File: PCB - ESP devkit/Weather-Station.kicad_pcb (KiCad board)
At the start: 2 copper layers, 39 parts, among them J1 Biruta, J10 Conn_01x19, J11 Conn_01x19, J2 Power, J3 BH1750-FVI, J4 BME280, J5 Pluviometro, J6 Anemometro, J7 FTDI, J8 Conn_01x02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

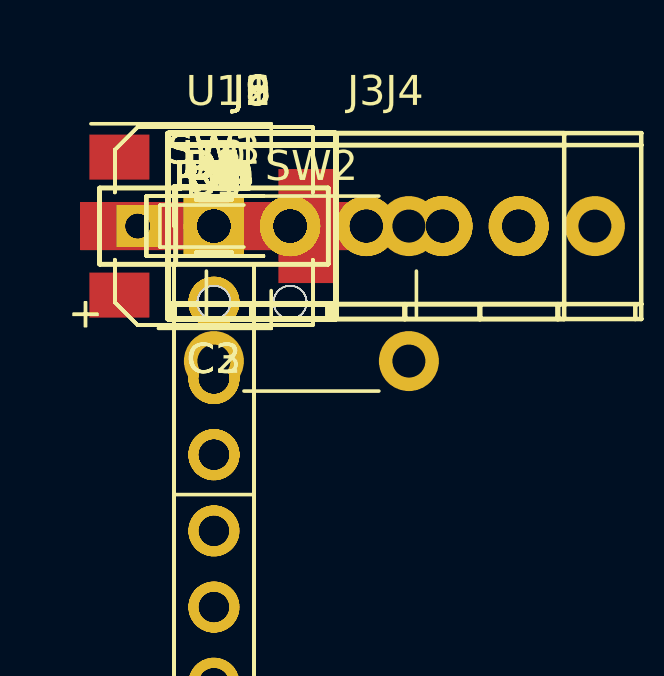
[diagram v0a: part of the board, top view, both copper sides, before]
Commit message: Tirando o circuito de programação do ESP
Signed-off-by: Gustavo Costa <gustavocosta@ic.ufal.br>
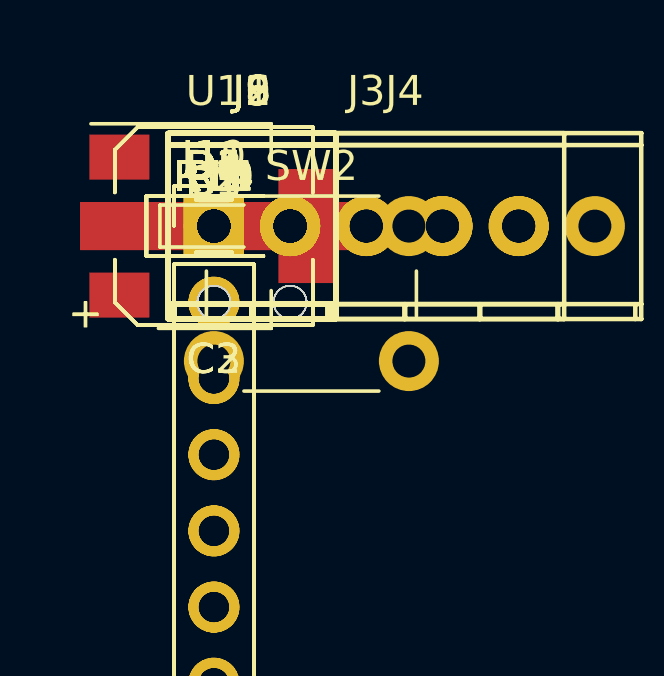
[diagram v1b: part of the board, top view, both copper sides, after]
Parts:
- removed J7: FTDI, Pin_Headers:Pin_Header_Straight_1x04_Pitch2.54mm
- removed R16, R4, R6, R8: 10K, Resistors_SMD:R_0805
- removed SW1: SW_Push_SPDT, Buttons_Switches_ThroughHole:SW_Micro_SPST
- removed SW3: SW_SPDT, Buttons_Switches_ThroughHole:SW_Micro_SPST
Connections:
- C3 pad 1: Net-(C3-Pad1) -> +3V3
- J10 pad 13: Net-(J10-Pad13) -> (no net)
- J11 pad 15: RXD -> (no net)
- J11 pad 16: TXD -> (no net)
- J11 pad 4: Net-(J11-Pad4) -> (no net)
- J11 pad 5: Net-(J11-Pad5) -> (no net)
- J11 pad 6: Net-(J11-Pad6) -> (no net)
- U1 pad 2: Net-(C3-Pad1) -> +3V3

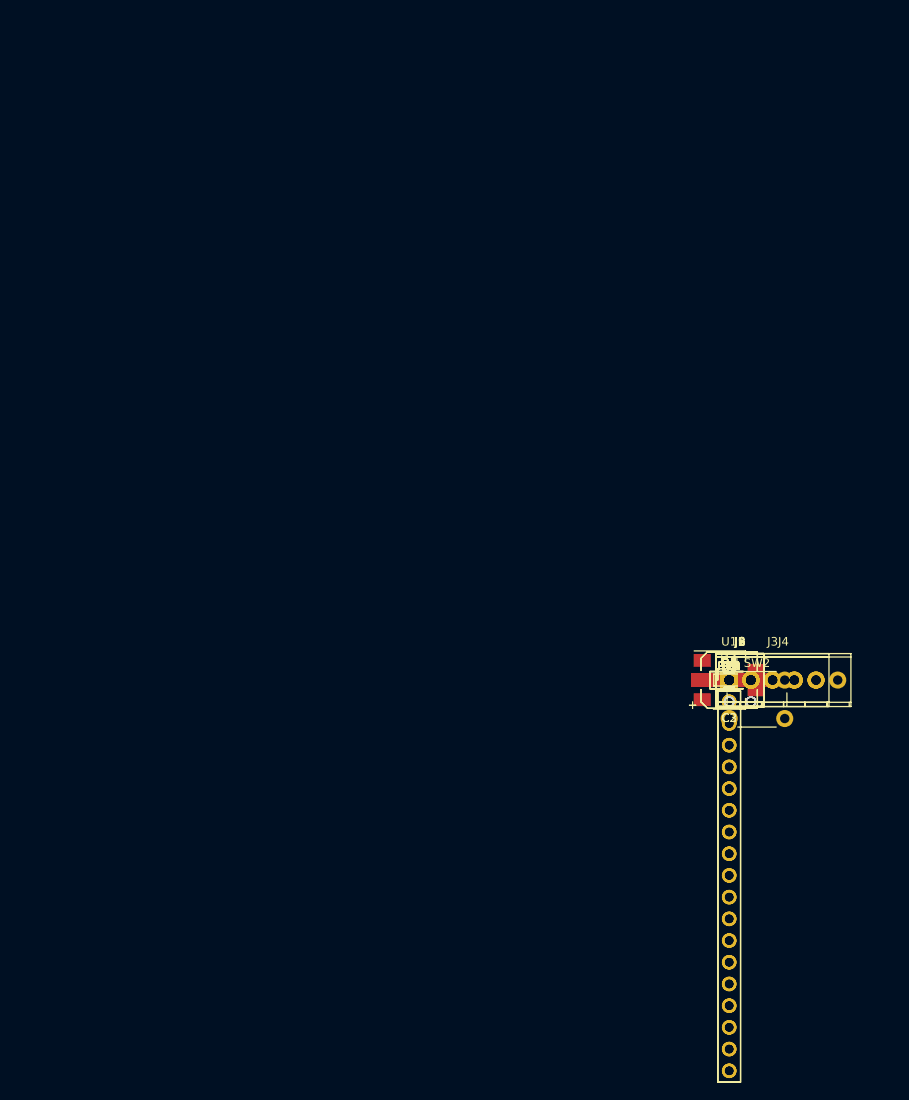
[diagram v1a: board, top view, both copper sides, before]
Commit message: Feita a PCB com ESP32 devkit
Signed-off-by: Gustavo Costa <gustavocosta@ic.ufal.br>
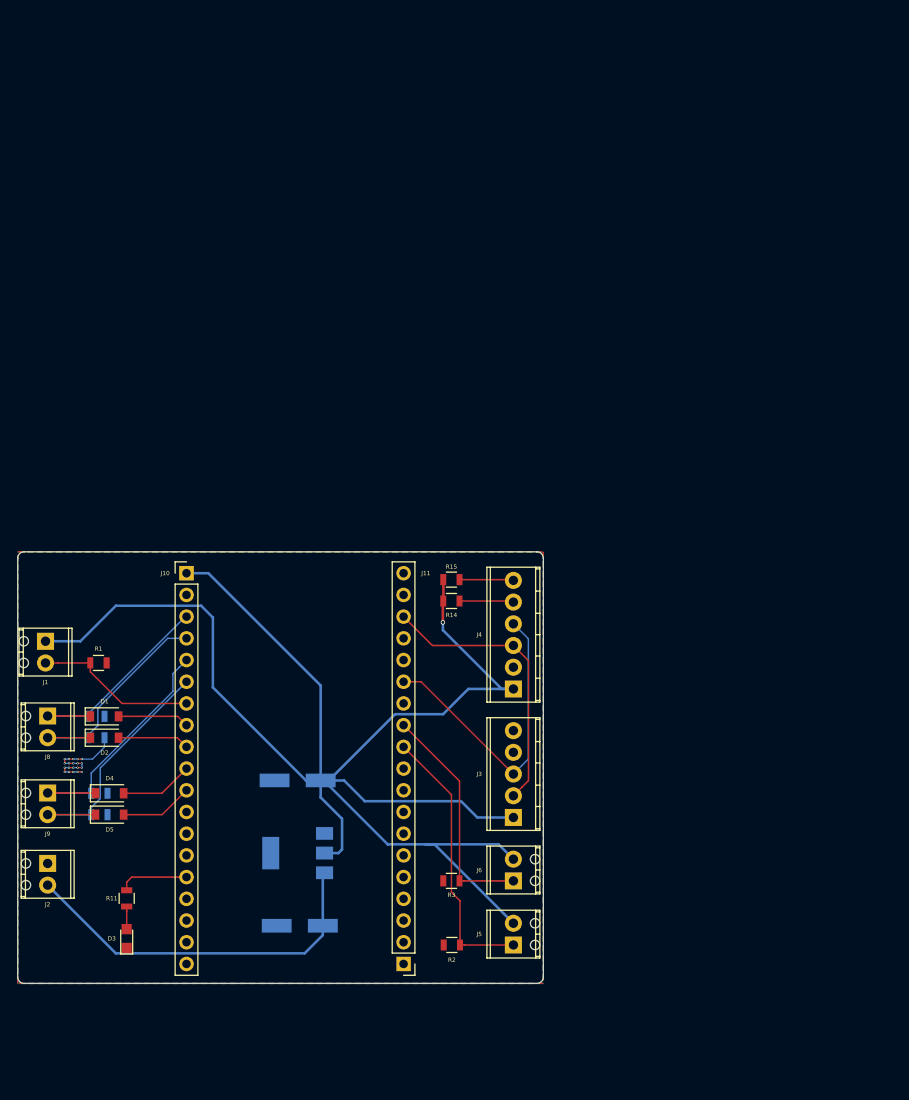
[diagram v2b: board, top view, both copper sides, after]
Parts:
- removed C1: 100nF, Capacitors_SMD:C_0805
- removed R5, R7: 10K, Resistors_SMD:R_0805
- removed SW2: SW_Push, Buttons_Switches_THT:SW_PUSH_6mm
- C2, C3, R10, R12, R13, R9, U1: moved to B.Cu
- moved J2 82.6 mm to (68.8, 126.5), turned to 270 degrees
- moved J9 80.8 mm to (68.8, 118.2), turned to 270 degrees
- moved J1 80.1 mm to (68.5, 100.5), turned to 270 degrees
- moved J8 79.9 mm to (68.8, 109.2), turned to 270 degrees
- moved D3 76.7 mm to (78.0, 135.2), turned to 90 degrees
- moved R13 75.4 mm to (74.8, 120.8)
- moved R11 75.0 mm to (78.0, 130.6), turned to 270 degrees
- moved R12 74.9 mm to (74.8, 118.2)
- moved R10 74.4 mm to (74.5, 111.8)
- moved D5 74.2 mm to (76.0, 120.8)
- moved R9 74.2 mm to (74.5, 109.2)
- moved R1 73.8 mm to (74.7, 103.0)
- moved D4 73.7 mm to (76.0, 118.2)
- moved D2 73.4 mm to (75.4, 111.8)
- moved D1 73.2 mm to (75.4, 109.2)
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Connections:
- J10 pad 2: Net-(C1-Pad2) -> (no net)
- J11 pad 10: Net-(J11-Pad10) -> (no net)
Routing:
- net +3V3: track 0.00 -> 200.5 mm, vias 0 -> 1
- net Net-(C2-Pad1): track 0.00 -> 43.8 mm
- net Net-(J11-Pad14): track 0.00 -> 36.4 mm
- net Net-(J11-Pad17): track 0.00 -> 33.3 mm
- net Net-(J11-Pad11): track 0.00 -> 32.2 mm
- net ADC1_CH6: track 0.00 -> 30.9 mm
- net ADC1_CH7: track 0.00 -> 30.9 mm
- net Net-(J11-Pad12): track 0.00 -> 27.2 mm
- net ADC1_CH3: track 0.00 -> 26.9 mm
- net ADC1_CH0: track 0.00 -> 25.8 mm
- net ADC1_CH4: track 0.00 -> 19.1 mm
- net GND: track 0.00 -> 13.8 mm, vias 0 -> 20
- net GPIO26: track 0.00 -> 8.55 mm
- net GPIO27: track 0.00 -> 8.53 mm
- net GPIO25: track 0.00 -> 8.39 mm
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- added copper zone on B.Cu, net GND
- added copper zone on F.Cu, net GND
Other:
- board outline added: 61.5 x 50.5 mm

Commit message: Ajustando PCBs
Signed-off-by: Gustavo Costa <gustavocosta@ic.ufal.br>
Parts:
- removed D1, D2, D4, D5: D, Diodes_SMD:D_SOD-123
- removed J1: Biruta, TerminalBlock_Phoenix:TerminalBlock_Phoenix_MPT-2.54mm_2pol
- removed J2: Power, TerminalBlock_Phoenix:TerminalBlock_Phoenix_MPT-2.54mm_2pol
- removed J5: Pluviometro, TerminalBlock_Phoenix:TerminalBlock_Phoenix_MPT-2.54mm_2pol
- removed J6: Anemometro, TerminalBlock_Phoenix:TerminalBlock_Phoenix_MPT-2.54mm_2pol
- removed R12, R13: 1.5K, Resistors_SMD:R_0805
- added Anemometro: Anemometro, TerminalBlock_Phoenix:TerminalBlock_Phoenix_MPT-2.54mm_2pol, F.Cu at (106.0, 55.5)
- added Biruta: Biruta, TerminalBlock_Phoenix:TerminalBlock_Phoenix_MPT-2.54mm_2pol, F.Cu at (106.0, 42.2)
- added C4: 22μF, Capacitors_SMD:CP_Elec_6.3x7.7, B.Cu at (115.5, 84.2)
- added C5: 22μF, Capacitors_SMD:CP_Elec_6.3x7.7, B.Cu at (131.0, 84.2)
- added C6: 0.1uF, Capacitors_SMD:C_0805, F.Cu at (117.2, 85.5)
- added C7: 0.1uF, Capacitors_SMD:C_0805, F.Cu at (133.2, 85.5)
- added C8: 0.1uF, Capacitors_SMD:C_0805, F.Cu at (149.2, 85.5)
- added C9: 0.1uF, Capacitors_SMD:C_0805, F.Cu at (165.2, 85.5)
- added J12: Conn_01x02, TerminalBlock_Phoenix:TerminalBlock_Phoenix_MPT-2.54mm_2pol, F.Cu at (137.8, 91.5)
- added J13: Conn_01x02, TerminalBlock_Phoenix:TerminalBlock_Phoenix_MPT-2.54mm_2pol, F.Cu at (145.8, 91.5)
- added J14: Conn_01x02, TerminalBlock_Phoenix:TerminalBlock_Phoenix_MPT-2.54mm_2pol, F.Cu at (153.8, 91.5)
- added J15: Conn_01x02, TerminalBlock_Phoenix:TerminalBlock_Phoenix_MPT-2.54mm_2pol, F.Cu at (161.8, 91.5)
- added J16: Conn_01x19, Pin_Headers:Pin_Header_Straight_1x19_Pitch2.54mm, F.Cu at (146.4, 31.0)
- added J7: Conn_01x19, Pin_Headers:Pin_Header_Straight_1x19_Pitch2.54mm, F.Cu at (121.0, 31.0)
- added Pluviometro: Pluviometro, TerminalBlock_Phoenix:TerminalBlock_Phoenix_MPT-2.54mm_2pol, F.Cu at (106.0, 48.8)
- added Power: Power, TerminalBlock_Phoenix:TerminalBlock_Phoenix_PT-3.5mm_2pol, F.Cu at (107.2, 71.0)
- added U3: AP1117-33, TO_SOT_Packages_SMD:SOT-223, B.Cu at (123.2, 84.0)
- added U4: ADS1115, Housings_SSOP:MSOP-10_3x3mm_Pitch0.5mm, F.Cu at (111.2, 84.5)
- added U5: ADS1115, Housings_SSOP:MSOP-10_3x3mm_Pitch0.5mm, F.Cu at (127.0, 84.5)
- added U6: ADS1115, Housings_SSOP:MSOP-10_3x3mm_Pitch0.5mm, F.Cu at (143.0, 84.5)
- added U7: ADS1115, Housings_SSOP:MSOP-10_3x3mm_Pitch0.5mm, F.Cu at (158.8, 84.5)
- J10, J11: value Conn_01x19 -> Conn_01x02; footprint Pin_Headers:Pin_Header_Straight_1x19_Pitch2.54mm -> TerminalBlock_Phoenix:TerminalBlock_Phoenix_MPT-2.54mm_2pol
- J3: value BH1750-FVI -> DataLogger; footprint TerminalBlock_Phoenix:TerminalBlock_Phoenix_MPT-2.54mm_5pol -> Pin_Headers:Pin_Header_Straight_1x08_Pitch2.54mm; moved to B.Cu
- R10, R9: value 1.5K -> 10k; moved to F.Cu
- moved R2 87.3 mm to (114.2, 48.8), turned to 180 degrees
- moved J4 86.0 mm to (165.3, 31.0), turned to 180 degrees
- moved J3 77.2 mm to (134.0, 44.6), turned to 180 degrees
- moved R10 76.9 mm to (128.8, 57.2)
- moved R9 76.9 mm to (128.8, 54.8)
- moved D3 74.8 mm to (107.5, 66.5), turned to 0 degrees
- moved R11 73.6 mm to (114.2, 66.5), turned to 180 degrees
- moved R3 73.0 mm to (114.2, 55.5), turned to 0 degrees
- moved C2 70.7 mm to (113.8, 64.8), turned to 0 degrees
- moved R1 70.4 mm to (114.2, 44.8)
- moved R14 70.2 mm to (155.2, 37.5), turned to 270 degrees
- moved U1 70.0 mm to (113.8, 57.0)
- moved C3 69.3 mm to (113.8, 49.2), turned to 0 degrees
- moved R15 66.6 mm to (152.5, 37.5), turned to 270 degrees
- moved J9 52.3 mm to (113.8, 91.5), turned to 0 degrees
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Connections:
- J10 pad 1: +3V3 -> Net-(J10-Pad1)
- J10 pad 2: (no net) -> Net-(J10-Pad2)
- J11 pad 1: (no net) -> Net-(J11-Pad1)
- J11 pad 2: (no net) -> Net-(J11-Pad2)
- J3 pad 1: +3V3 -> CS
- J3 pad 2: Net-(J11-Pad17) -> MOSI
- J3 pad 3: Net-(J11-Pad14) -> MISO
- J3 pad 4: (no net) -> SCK
- J3 pad 5: GND -> SCL
- J4 pad 3: Net-(J11-Pad17) -> SCL
- J4 pad 4: Net-(J11-Pad14) -> SDA
- J8 pad 1: ADC1_CH0 -> Net-(J8-Pad1)
- J8 pad 2: ADC1_CH3 -> Net-(J8-Pad2)
- J9 pad 1: ADC1_CH6 -> Net-(J9-Pad1)
- J9 pad 2: ADC1_CH7 -> Net-(J9-Pad2)
- R1 pad 1: ADC1_CH4 -> Net-(J1-Pad2)
- R10 pad 1: ADC1_CH3 -> +5V
- R10 pad 2: GND -> SDA
- R11 pad 1: Net-(J10-Pad15) -> Net-(J7-Pad15)
- R2 pad 2: Net-(J11-Pad11) -> Net-(J5-Pad1)
- R3 pad 1: Net-(J11-Pad12) -> Net-(J6-Pad1)
- R9 pad 1: ADC1_CH0 -> +5V
- R9 pad 2: GND -> SCL
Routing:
- net +5V: track 0.00 -> 157.6 mm, vias 0 -> 5
- net SCL: track 0.00 -> 136.1 mm, vias 0 -> 2
- net SDA: track 0.00 -> 125.4 mm, vias 0 -> 2
- net +3V3: track 200.5 -> 132.4 mm
- net Net-(J11-Pad14): track 36.4 -> 0.00 mm
- net Net-(J11-Pad17): track 33.3 -> 0.00 mm
- net Net-(J11-Pad11): track 32.2 -> 0.00 mm
- net ADC1_CH6: track 30.9 -> 0.00 mm
- net ADC1_CH7: track 30.9 -> 0.00 mm
- net Net-(J11-Pad12): track 27.2 -> 0.00 mm
- net ADC1_CH3: track 26.9 -> 0.00 mm
- net ADC1_CH0: track 25.8 -> 0.00 mm
- net CS: track 0.00 -> 24.4 mm
- net ADC1_CH4: track 19.1 -> 0.00 mm
- net MOSI: track 0.00 -> 18.8 mm
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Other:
- board size 61.5 x 50.5 mm -> 65 x 67.5 mm
- board text added: "+"
